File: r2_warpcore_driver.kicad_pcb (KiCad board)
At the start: 2 copper layers, 151 x 94.4 mm, 1 part, among them U1 ESP32-S3-MINI-1

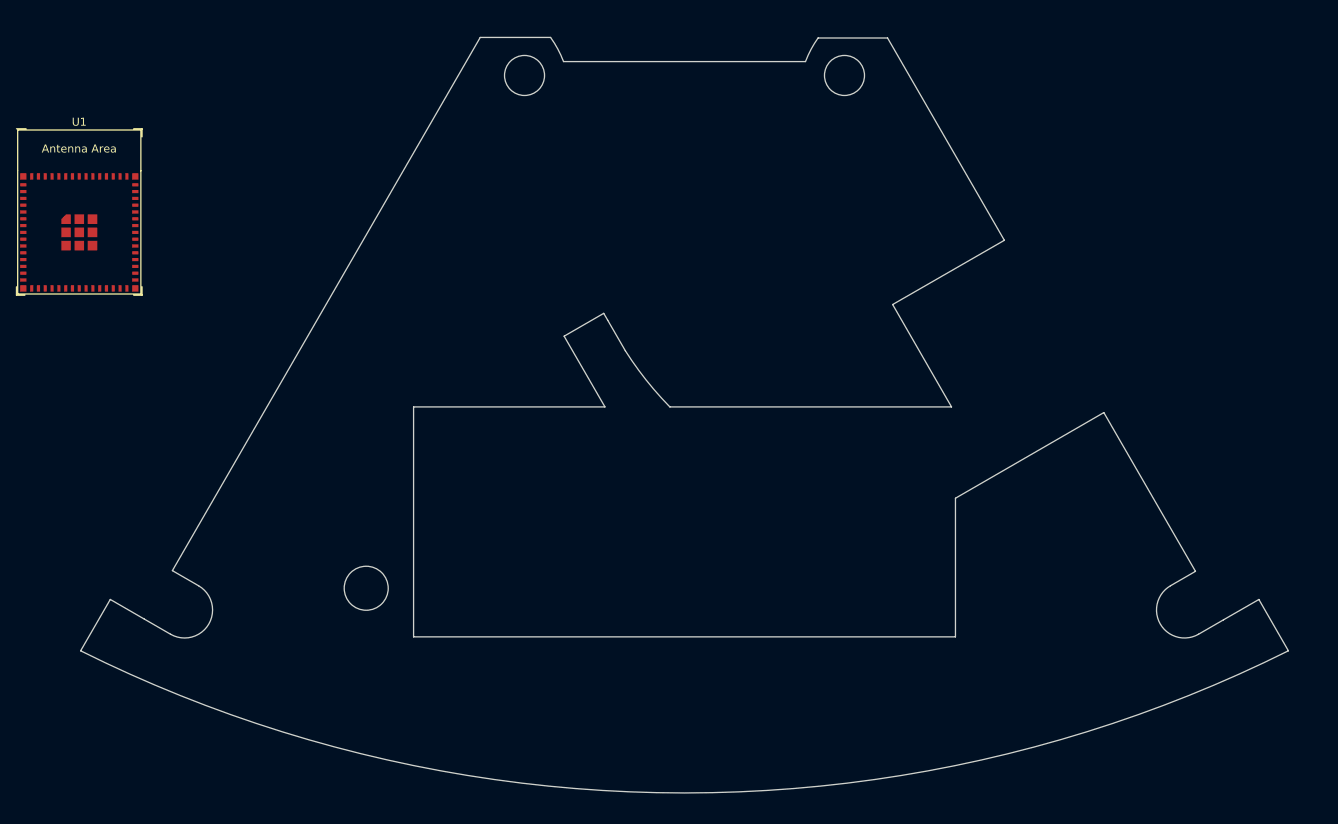
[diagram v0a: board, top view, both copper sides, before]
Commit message: Updates to build & adding hash insertion on PCB
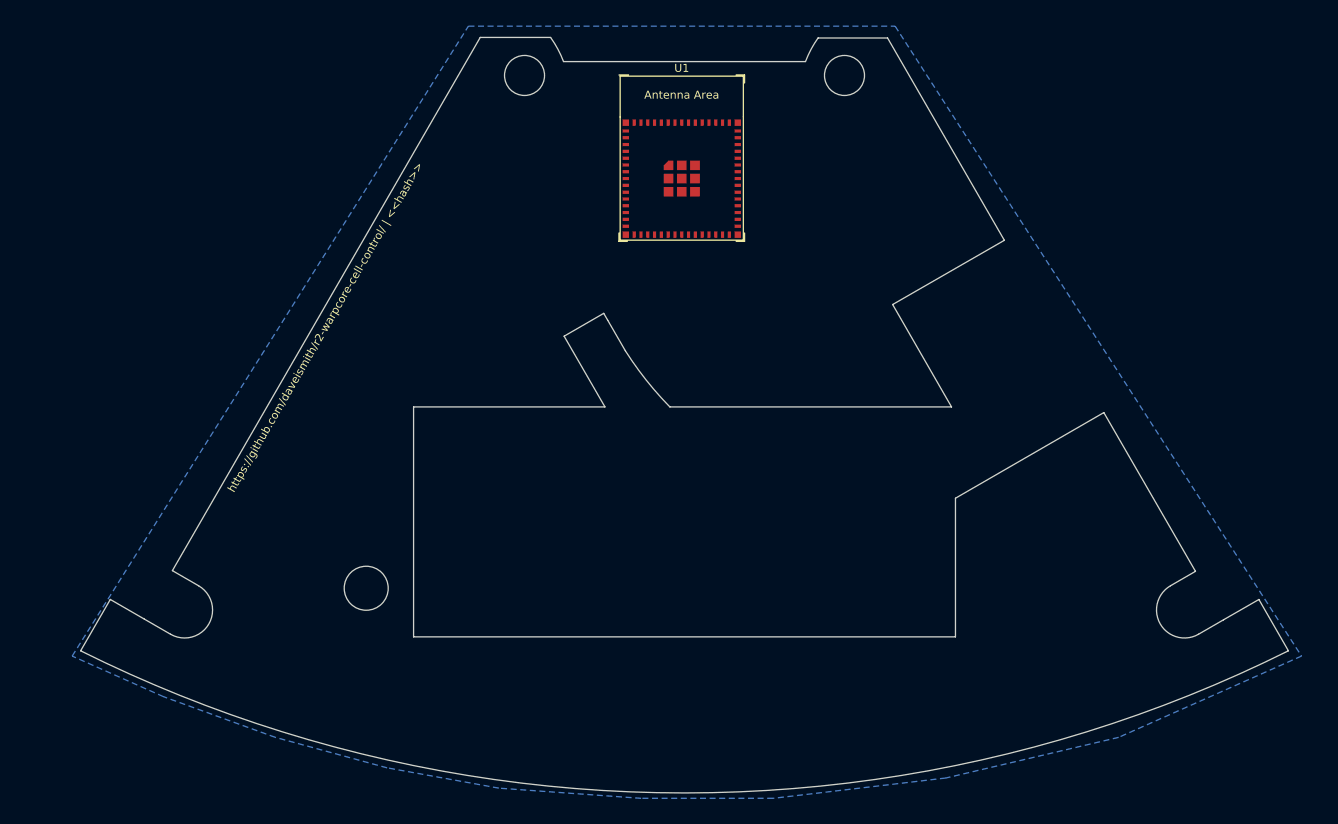
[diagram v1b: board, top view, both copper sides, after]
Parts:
- moved U1 75.6 mm to (157.5, 58.4)
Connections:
- net Net-(U1-GND-Pad1) renamed GND
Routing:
- added copper zone on B.Cu, net GND
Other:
- board text added: "https://github.com/daveismith/r2-warpcore-cell-control/ | <<hash>>"

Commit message: Updates with most of the layout completed. Still need to populate some JLCPCB parts and also need to specify the resistors for the LEDS. Should also review if we want to drive the LEDs directly from the MCU or if we want to put in some transistors to drive the LEDs from a higher voltage / current source.
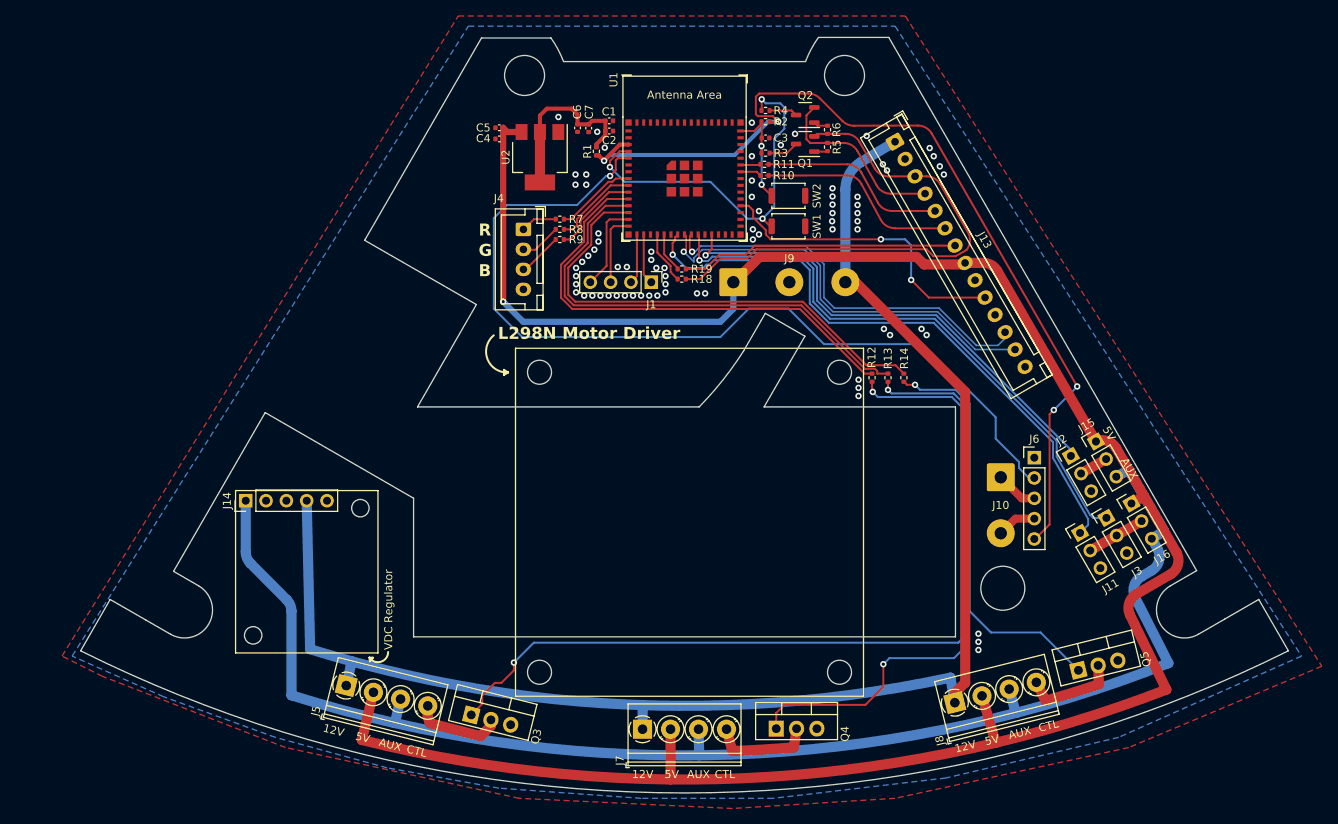
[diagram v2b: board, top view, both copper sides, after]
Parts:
- added C1: 10uF/25V(20%), Capacitor_SMD:C_0402_1005Metric, F.Cu at (148.4, 51.2)
- added C2: 0.1uF/50V(10%), Capacitor_SMD:C_0402_1005Metric, F.Cu at (148.4, 52.5)
- added C3: 1uF/16V(10%), Capacitor_SMD:C_0402_1005Metric, F.Cu at (168.0, 53.3)
- added C4: 10uF/25V(20%), Capacitor_SMD:C_0402_1005Metric, F.Cu at (134.7, 53.5)
- added C5: 0.1uF/50V(10%), Capacitor_SMD:C_0402_1005Metric, F.Cu at (134.7, 52.1)
- added C6: 0.1uF/50V(10%), Capacitor_SMD:C_0402_1005Metric, F.Cu at (144.4, 52.1)
- added C7: 10uF/25V(20%), Capacitor_SMD:C_0402_1005Metric, F.Cu at (145.8, 52.1)
- added J1: Conn_01x04_Pin, Connector_PinHeader_2.54mm:PinHeader_1x04_P2.54mm_Vertical, F.Cu at (153.7, 71.4)
- added J10: Screw_Terminal_01x02, Connector_Wire:SolderWire-0.75sqmm_1x02_P7mm_D1.25mm_OD3.5mm, F.Cu at (197.4, 95.8)
- added J11: Conn_01x03_Pin, Connector_PinHeader_2.54mm:PinHeader_1x03_P2.54mm_Vertical, F.Cu at (207.3, 102.7)
- added J13: Conn_01x14_Pin, Connector_JST:JST_XH_B14B-XH-A_1x14_P2.50mm_Vertical, F.Cu at (184.1, 53.8)
- added J14: Conn_01x05_Pin, Connector_PinHeader_2.54mm:PinHeader_1x05_P2.54mm_Vertical, F.Cu at (103.0, 98.7)
- added J15: Conn_01x03_Pin, Connector_PinHeader_2.54mm:PinHeader_1x03_P2.54mm_Vertical, F.Cu at (209.3, 91.3)
- added J16: Conn_01x03_Pin, Connector_PinHeader_2.54mm:PinHeader_1x03_P2.54mm_Vertical, F.Cu at (213.7, 99.0)
- added J2: Conn_01x03_Pin, Connector_PinHeader_2.54mm:PinHeader_1x03_P2.54mm_Vertical, F.Cu at (206.1, 93.1)
- added J3: Conn_01x03_Pin, Connector_PinHeader_2.54mm:PinHeader_1x03_P2.54mm_Vertical, F.Cu at (210.6, 100.8)
- added J4: Conn_01x04_Pin, Connector_JST:JST_XH_B4B-XH-A_1x04_P2.50mm_Vertical, F.Cu at (137.7, 64.8)
- added J5: Screw_Terminal_01x04, TerminalBlock_Phoenix:TerminalBlock_Phoenix_PT-1,5-4-3.5-H_1x04_P3.50mm_Horizontal, F.Cu at (115.5, 121.8)
- added J6: Conn_01x05_Pin, Connector_PinHeader_2.54mm:PinHeader_1x05_P2.54mm_Vertical, F.Cu at (201.5, 93.3)
- added J7: Screw_Terminal_01x04, TerminalBlock_Phoenix:TerminalBlock_Phoenix_PT-1,5-4-3.5-H_1x04_P3.50mm_Horizontal, F.Cu at (152.6, 127.3)
- added J8: Screw_Terminal_01x04, TerminalBlock_Phoenix:TerminalBlock_Phoenix_PT-1,5-4-3.5-H_1x04_P3.50mm_Horizontal, F.Cu at (191.6, 123.9)
- added J9: Screw_Terminal_01x03, Connector_Wire:SolderWire-0.75sqmm_1x03_P7mm_D1.25mm_OD3.5mm, F.Cu at (163.9, 71.4)
- added Q1: L8050QLT1G, Package_TO_SOT_SMD:SOT-23-3, F.Cu at (172.9, 54.1)
- added Q2: L8050QLT1G, Package_TO_SOT_SMD:SOT-23-3, F.Cu at (172.9, 50.5)
- added Q3: IRLB8721PBF, Package_TO_SOT_THT:TO-220-3_Vertical, F.Cu at (131.2, 125.5)
- added Q4: IRLB8721PBF, Package_TO_SOT_THT:TO-220-3_Vertical, F.Cu at (169.3, 127.2)
- added Q5: IRLB8721PBF, Package_TO_SOT_THT:TO-220-3_Vertical, F.Cu at (207.1, 119.9)
- added R1: 0(1%), Resistor_SMD:R_0402_1005Metric, F.Cu at (146.8, 55.0)
- added R10: 0(1%), Resistor_SMD:R_0402_1005Metric, F.Cu at (167.8, 58.0)
- added R11: 0(1%), Resistor_SMD:R_0402_1005Metric, F.Cu at (167.8, 56.6)
- added R12: 0(1%), Resistor_SMD:R_0402_1005Metric, F.Cu at (181.3, 83.3)
- added R13: 0(1%), Resistor_SMD:R_0402_1005Metric, F.Cu at (183.3, 83.3)
- added R14: 0(1%), Resistor_SMD:R_0402_1005Metric, F.Cu at (185.2, 83.3)
- added R18: 0(1%), Resistor_SMD:R_0402_1005Metric, F.Cu at (157.5, 71.0)
- added R19: 0(1%), Resistor_SMD:R_0402_1005Metric, F.Cu at (157.5, 69.7)
- added R2: 10K(1%), Resistor_SMD:R_0402_1005Metric, F.Cu at (168.0, 51.3)
- added R3: 0(1%), Resistor_SMD:R_0402_1005Metric, F.Cu at (168.0, 55.2)
- added R4: 0(1%), Resistor_SMD:R_0402_1005Metric, F.Cu at (168.0, 49.9)
- added R5: 10K(1%), Resistor_SMD:R_0402_1005Metric, F.Cu at (175.7, 54.5)
- added R6: 10K(1%), Resistor_SMD:R_0402_1005Metric, F.Cu at (175.7, 52.3)
- added R7: R, Resistor_SMD:R_0402_1005Metric, F.Cu at (142.2, 63.5)
- added R8: R, Resistor_SMD:R_0402_1005Metric, F.Cu at (142.2, 64.8)
- added R9: R, Resistor_SMD:R_0402_1005Metric, F.Cu at (142.2, 66.0)
- added SW1: SW_Push, Button_Switch_SMD:SW_Push_SPST_NO_Alps_SKRK, F.Cu at (170.8, 64.4)
- added SW2: SW_Push, Button_Switch_SMD:SW_Push_SPST_NO_Alps_SKRK, F.Cu at (170.8, 60.6)
- added U2: AP1117-33, Package_TO_SOT_SMD:SOT-223-3_TabPin2, F.Cu at (139.8, 55.8)
- moved U1 0.35 mm to (157.8, 58.4)
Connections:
- U1 pad 10: unconnected-(U1-GPIO6/TOUCH6/ADC1_CH5-Pad10) -> /LED_B
- U1 pad 11: unconnected-(U1-GPIO7/TOUCH7/ADC1_CH6-Pad11) -> /FET1
- U1 pad 12: unconnected-(U1-GPIO8/TOUCH8/ADC1_CH7/SUBSPICS1-Pad12) -> /FET2
- U1 pad 13: unconnected-(U1-GPIO9/TOUCH9/ADC1_CH8/FSPIHD/SUBSPIHD-Pad13) -> /FET3
- U1 pad 14: unconnected-(U1-GPIO10/TOUCH10/ADC1_CH9/FSPICS0/FSPIIO4/SUBSPICS0-Pad14) -> /MC_IN4
- U1 pad 15: unconnected-(U1-GPIO11/TOUCH11/ADC2_CH0/FSPID/FSPIIO5/SUBSPID-Pad15) -> /MC_IN3
- U1 pad 16: unconnected-(U1-GPIO12/TOUCH12/ADC2_CH1/FSPICLK/FSPIIO6/SUBSPICLK-Pad16) -> /MC_IN2
- U1 pad 17: unconnected-(U1-GPIO13/TOUCH13/ADC2_CH2/FSPIQ/FSPIIO7/SUBSPIQ-Pad17) -> /MC_IN1
- U1 pad 19: unconnected-(U1-GPIO15/U0RTS/ADC2_CH4/XTAL_32K_P-Pad19) -> /ESP_RTS
- U1 pad 20: unconnected-(U1-GPIO16/U0CTS/ADC2_CH5/XTAL_32K_N-Pad20) -> /ESP_CTS
- U1 pad 22: unconnected-(U1-GPIO18/U1RXD/ADC2_CH7/CLK_OUT3-Pad22) -> /SERVO3
- U1 pad 23: unconnected-(U1-GPIO19/U1RTS/ADC2_CH8/CLK_OUT2/USB_D--Pad23) -> /D-
- U1 pad 24: unconnected-(U1-GPIO20/U1CTS/ADC2_CH9/CLK_OUT1/USB_D+-Pad24) -> /D+
- U1 pad 25: unconnected-(U1-GPIO21-Pad25) -> /SERVO2
- U1 pad 27: unconnected-(U1-GPIO47/SPICLK_P/SUBSPICLK_P_DIFF-Pad27) -> /SERVO1
- U1 pad 3: unconnected-(U1-3V3-Pad3) -> /ESP_3V3
- U1 pad 34: unconnected-(U1-GPIO38/FSPIWP/SUBSPIWP-Pad34) -> /ID
- U1 pad 39: unconnected-(U1-U0TXD/GPIO43/CLK_OUT1-Pad39) -> /ESP_TXD
- U1 pad 4: unconnected-(U1-GPIO0/BOOT-Pad4) -> /GPIO0
- U1 pad 40: unconnected-(U1-U0RXD/GPIO44/CLK_OUT2-Pad40) -> /ESP_RXD
- U1 pad 45: unconnected-(U1-EN-Pad45) -> /CHIP_PU
- U1 pad 5: unconnected-(U1-GPIO1/TOUCH1/ADC1_CH0-Pad5) -> /ACT_POS
- U1 pad 8: unconnected-(U1-GPIO4/TOUCH4/ADC1_CH3-Pad8) -> /LED_R
- U1 pad 9: unconnected-(U1-GPIO5/TOUCH5/ADC1_CH4-Pad9) -> /LED_G
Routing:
- net +5V: track 0.00 -> 279.3 mm, vias 0 -> 1
- net +12V: track 0.00 -> 189.3 mm
- net +VDC: track 0.00 -> 177.8 mm
- net /ESP_3V3: track 0.00 -> 117.1 mm, vias 0 -> 4
- net /ACT_POS: track 0.00 -> 113.0 mm, vias 0 -> 1
- net Net-(Q3-G): track 0.00 -> 108.7 mm, vias 0 -> 2
- net /SERVO3: track 0.00 -> 76.2 mm, vias 0 -> 1
- net /SERVO2: track 0.00 -> 72.8 mm, vias 0 -> 1
- net Net-(Q4-G): track 0.00 -> 72.4 mm, vias 0 -> 2
- net /RTS: track 0.00 -> 65.8 mm
- net /SERVO1: track 0.00 -> 62.2 mm, vias 0 -> 1
- net /FET3: track 0.00 -> 60.9 mm
- net /FET2: track 0.00 -> 60.6 mm
- net /FET1: track 0.00 -> 59.9 mm
- net /D-: track 0.00 -> 52.8 mm, vias 0 -> 1
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- added copper zone on F.Cu, net GND
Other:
- outline, holes or cut-outs redrawn
- board text added: "12V"
- board text added: "5V"
- board text added: "AUX"
- board text added: "B"
- board text added: "CTL"
- board text added: "G"
- board text added: "L298N Motor Driver"
- board text added: "R"
- board text added: "VDC Regulator"
- board text removed: "https://github.com/daveismith/r2-warpcore-cell-control/ | <<hash>>"

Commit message: Adding URL & git hash placeholder information in as well as a note for more todo
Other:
- board text added: "https://github.com/daveismith/r2-warpcore-cell-control @ <<hash>>"
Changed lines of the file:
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@@
   (gr_line (start 157.82637 -100) (end 157.82637 200)
     (stroke (width 0.15) (type default)) (layer "User.9"))
+  (gr_text "https://github.com/daveismith/r2-warpcore-cell-control\n@ <<hash>>" (at 204.216 84.582 -60) (layer "B.SilkS")
+    (effects (font (size 1 1) (thickness 0.15)) (justify left bottom mirror))
+  )
   (gr_text "VDC Regulator" (at 121.412 117.348 90) (layer "F.SilkS")
     (effects (font (size 1 1) (thickness 0.15)) (justify left bottom))

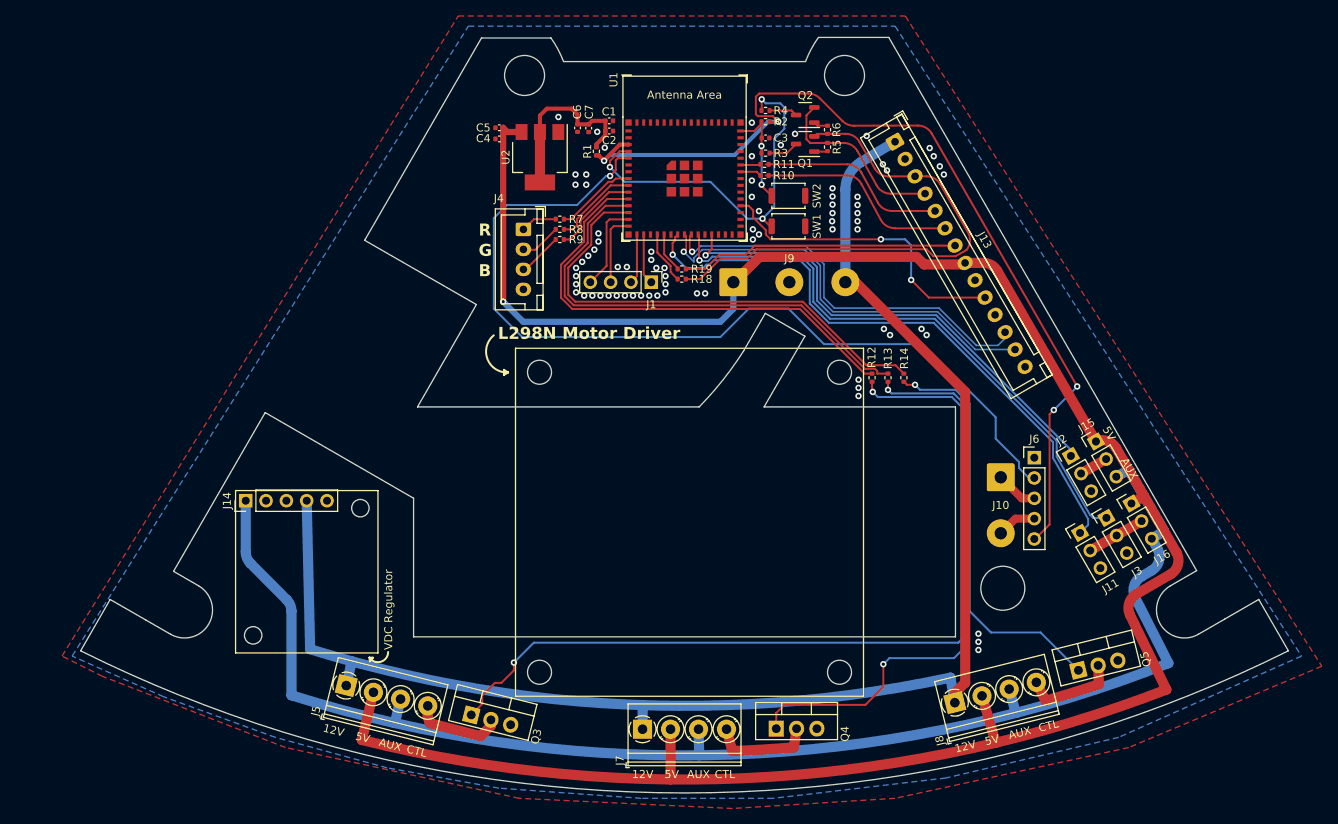
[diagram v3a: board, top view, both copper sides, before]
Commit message: Updating JLC parts, adding transistor drive for RGB, USB diodes
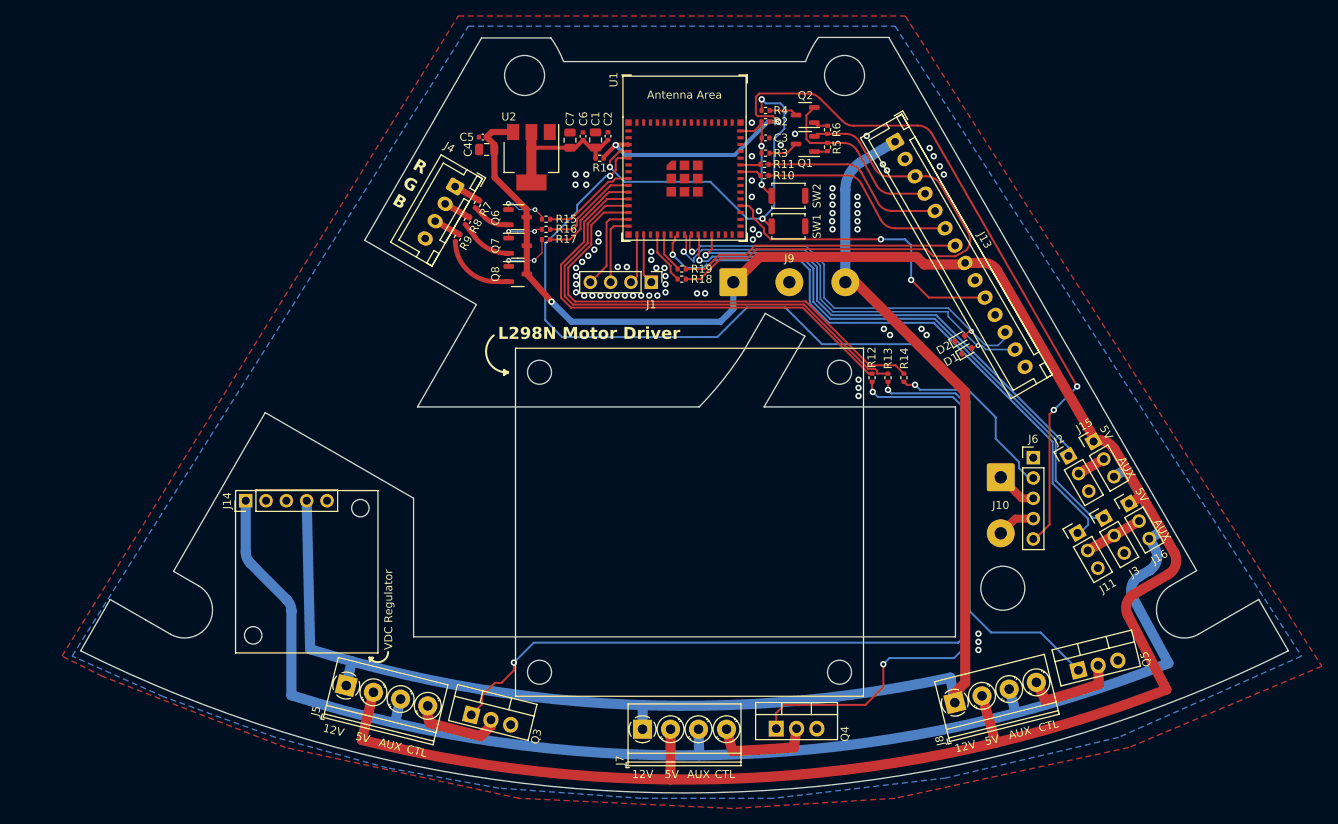
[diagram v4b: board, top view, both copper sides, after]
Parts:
- added D1: LESD5D5.0CT1G, Diode_SMD:D_SOD-523, F.Cu at (193.1, 80.0)
- added D2: LESD5D5.0CT1G, Diode_SMD:D_SOD-523, F.Cu at (192.2, 78.4)
- added Q6: Q_PNP_BEC, Package_TO_SOT_SMD:SOT-23-3, F.Cu at (137.0, 63.2)
- added Q7: Q_PNP_BEC, Package_TO_SOT_SMD:SOT-23-3, F.Cu at (137.0, 66.8)
- added Q8: Q_PNP_BEC, Package_TO_SOT_SMD:SOT-23-3, F.Cu at (137.0, 70.4)
- added R15: 1K(1%), Resistor_SMD:R_0402_1005Metric, F.Cu at (140.5, 63.5)
- added R16: 1K(1%), Resistor_SMD:R_0402_1005Metric, F.Cu at (140.5, 64.8)
- added R17: 1K(1%), Resistor_SMD:R_0402_1005Metric, F.Cu at (140.5, 66.0)
- C1, C4, C7: footprint Capacitor_SMD:C_0402_1005Metric -> Capacitor_SMD:C_0805_2012Metric
- R7: value R -> 200
- R8, R9: value R -> 100
- U2: value AP1117-33 -> LDL1117S33R
- moved R9 12.8 mm to (129.4, 65.9), turned to 60 degrees
- moved R8 11.6 mm to (130.7, 63.7), turned to 60 degrees
- moved R7 10.5 mm to (131.9, 61.6), turned to 60 degrees
- moved J4 10.1 mm to (129.2, 59.4), turned to -120 degrees
- moved C1 2.93 mm to (146.7, 53.6), turned to 90 degrees
- moved C7 2.78 mm to (143.5, 53.6), turned to 90 degrees
- moved C5 2.37 mm to (132.6, 53.2)
- moved C4 2.06 mm to (133.1, 54.8)
- moved C6 1.25 mm to (145.1, 53.1), turned to 90 degrees
- moved U2 1.07 mm to (138.7, 55.8)
- moved R1 0.95 mm to (147.2, 55.9), turned to 0 degrees
- moved C2 0.65 mm to (148.3, 53.1), turned to 90 degrees
- moved J11 0.32 mm to (207.0, 102.7)
- moved J16 0.32 mm to (213.4, 99.0)
- moved J3 0.32 mm to (210.2, 100.8)
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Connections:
- R7 pad 1: /LED_R -> Net-(Q6-E)
- R8 pad 1: /LED_G -> Net-(Q7-E)
- R9 pad 1: /LED_B -> Net-(Q8-E)
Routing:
- net /ACT_POS: track 113.0 -> 99.8 mm
- net Net-(Q8-E): track 0.00 -> 9.33 mm
- net Net-(Q8-B): track 0.00 -> 6.97 mm, vias 0 -> 2
- net Net-(Q7-E): track 0.00 -> 6.79 mm
- net Net-(Q6-B): track 0.00 -> 5.99 mm, vias 0 -> 2
- net Net-(Q7-B): track 0.00 -> 5.11 mm, vias 0 -> 2
- net Net-(Q6-E): track 0.00 -> 4.89 mm
- net +3V3: track 22.6 -> 18.6 mm
- net +5V: track 279.3 -> 276.5 mm
- net /ESP_3V3: track 117.1 -> 114.6 mm
- net /B: track 5.61 -> 3.46 mm
- net /LED_R: track 10.2 -> 11.9 mm
- net /LED_G: track 10.8 -> 12.5 mm
- net /LED_B: track 11.1 -> 12.9 mm
- net /G: track 5.11 -> 3.47 mm
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
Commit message: PCB Cleanup
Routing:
- net /SERVO1: track 62.2 -> 61.3 mm
- net /ACT_POS: track 99.8 -> 99.0 mm
- net /D+: track 52.1 -> 51.3 mm
- net +5V: track 276.5 -> 276.0 mm
- net /RTS: track 65.8 -> 65.3 mm
